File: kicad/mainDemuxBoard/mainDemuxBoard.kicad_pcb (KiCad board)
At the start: 2 copper layers, 217 parts, among them J1 Conn_02x20_Top_Bottom, J10 Conn_02x20_Top_Bottom, J11 Conn_02x20_Top_Bottom, J12 Conn_02x20_Top_Bottom, J13 Conn_02x20_Top_Bottom, J14 Conn_02x20_Top_Bottom, J15 Conn_02x20_Top_Bottom, J16 Conn_02x20_Top_Bottom, J17 Conn_02x20_Top_Bottom, J2 Conn_02x20_Top_Bottom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

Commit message: finish main demux board
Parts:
- moved J4 187.7 mm to (109.2, 105.0)
- moved J1 187.5 mm to (121.2, 105.0)
- moved J8 186.1 mm to (85.8, 105.0)
- moved J6 185.0 mm to (97.5, 105.0)
- moved J10 183.4 mm to (74.0, 105.0)
- moved J12 183.1 mm to (62.2, 105.0)
- moved J14 181.7 mm to (50.2, 105.0)
- moved J16 180.8 mm to (38.2, 105.0)
- moved J11 85.1 mm to (74.0, 32.0)
- moved J17 85.0 mm to (38.2, 32.0)
- moved J2 83.1 mm to (121.2, 32.0)
- moved J13 82.8 mm to (62.2, 32.0)
- moved J9 82.1 mm to (85.8, 32.0)
- moved J15 82.0 mm to (50.2, 32.0)
- moved J7 80.7 mm to (97.5, 32.0)
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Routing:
- net /S_{2}: track 0.00 -> 306.9 mm
- net /S_{3}: track 0.00 -> 297.1 mm, vias 0 -> 1
- net /S_{1}: track 0.00 -> 287.2 mm
- net /~{BL_{6}}: track 0.00 -> 284.4 mm, vias 0 -> 3
- net /BL_{1}: track 0.00 -> 284.2 mm
- net /~{BL_{5}}: track 0.00 -> 283.0 mm, vias 0 -> 2
- net /S_{0}: track 0.00 -> 281.1 mm
- net /~{BL_{4}}: track 0.00 -> 281.1 mm, vias 0 -> 1
- net /~{BL_{2}}: track 0.00 -> 278.9 mm, vias 0 -> 1
- net /~{BL_{0}}: track 0.00 -> 277.4 mm
- net /~{BL_{7}}: track 0.00 -> 277.2 mm
- net /~{BL_{1}}: track 0.00 -> 276.9 mm, vias 0 -> 2
- net /BL_{5}: track 0.00 -> 276.6 mm, vias 0 -> 1
- net /BL_{7}: track 0.00 -> 274.5 mm, vias 0 -> 2
- net /BL_{3}: track 0.00 -> 272.5 mm, vias 0 -> 1
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- added copper zone on In2.Cu, net +10V
- added copper zone on In2.Cu, net +5V
- added copper zone on In1.Cu, net GND
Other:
- board outline added: 150 x 150 mm
- copper layers 2 -> 4

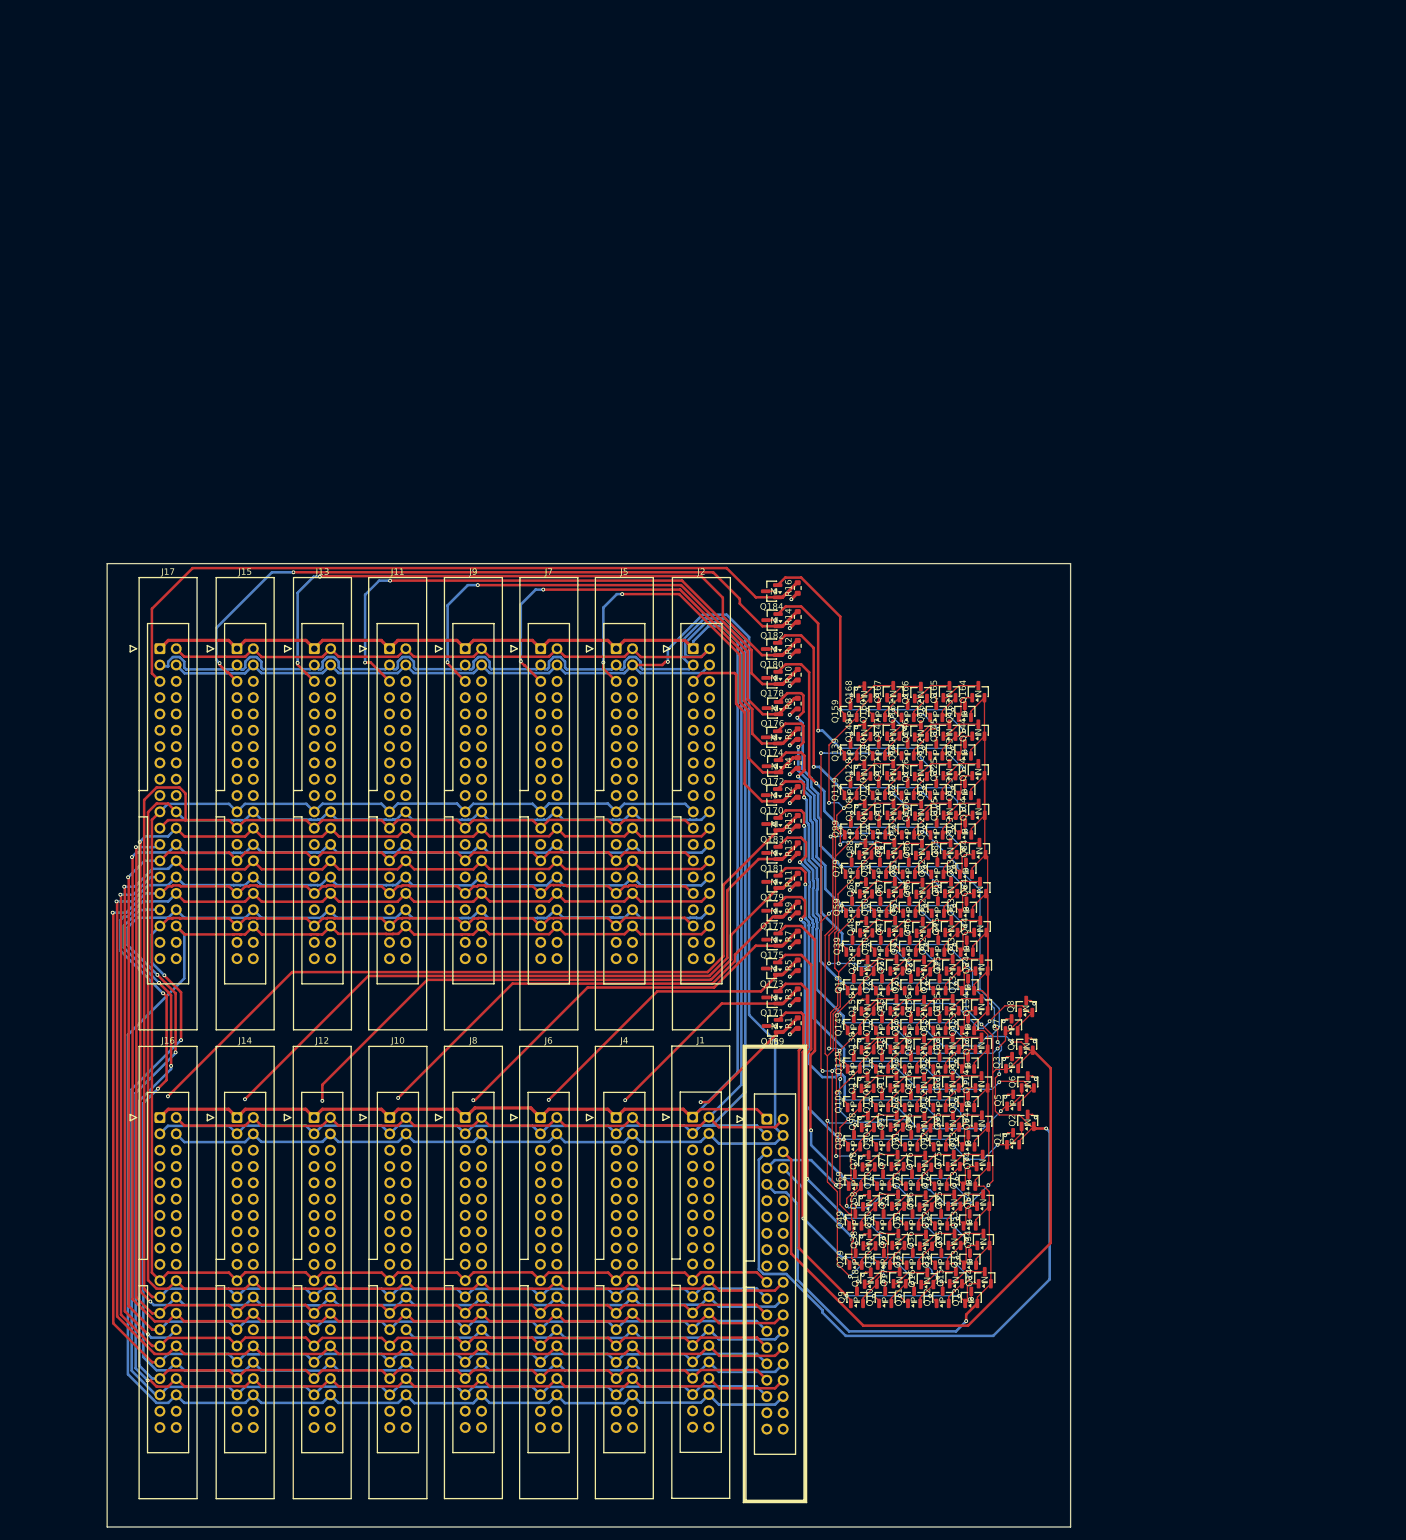
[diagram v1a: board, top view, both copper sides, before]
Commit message: update main board schematic
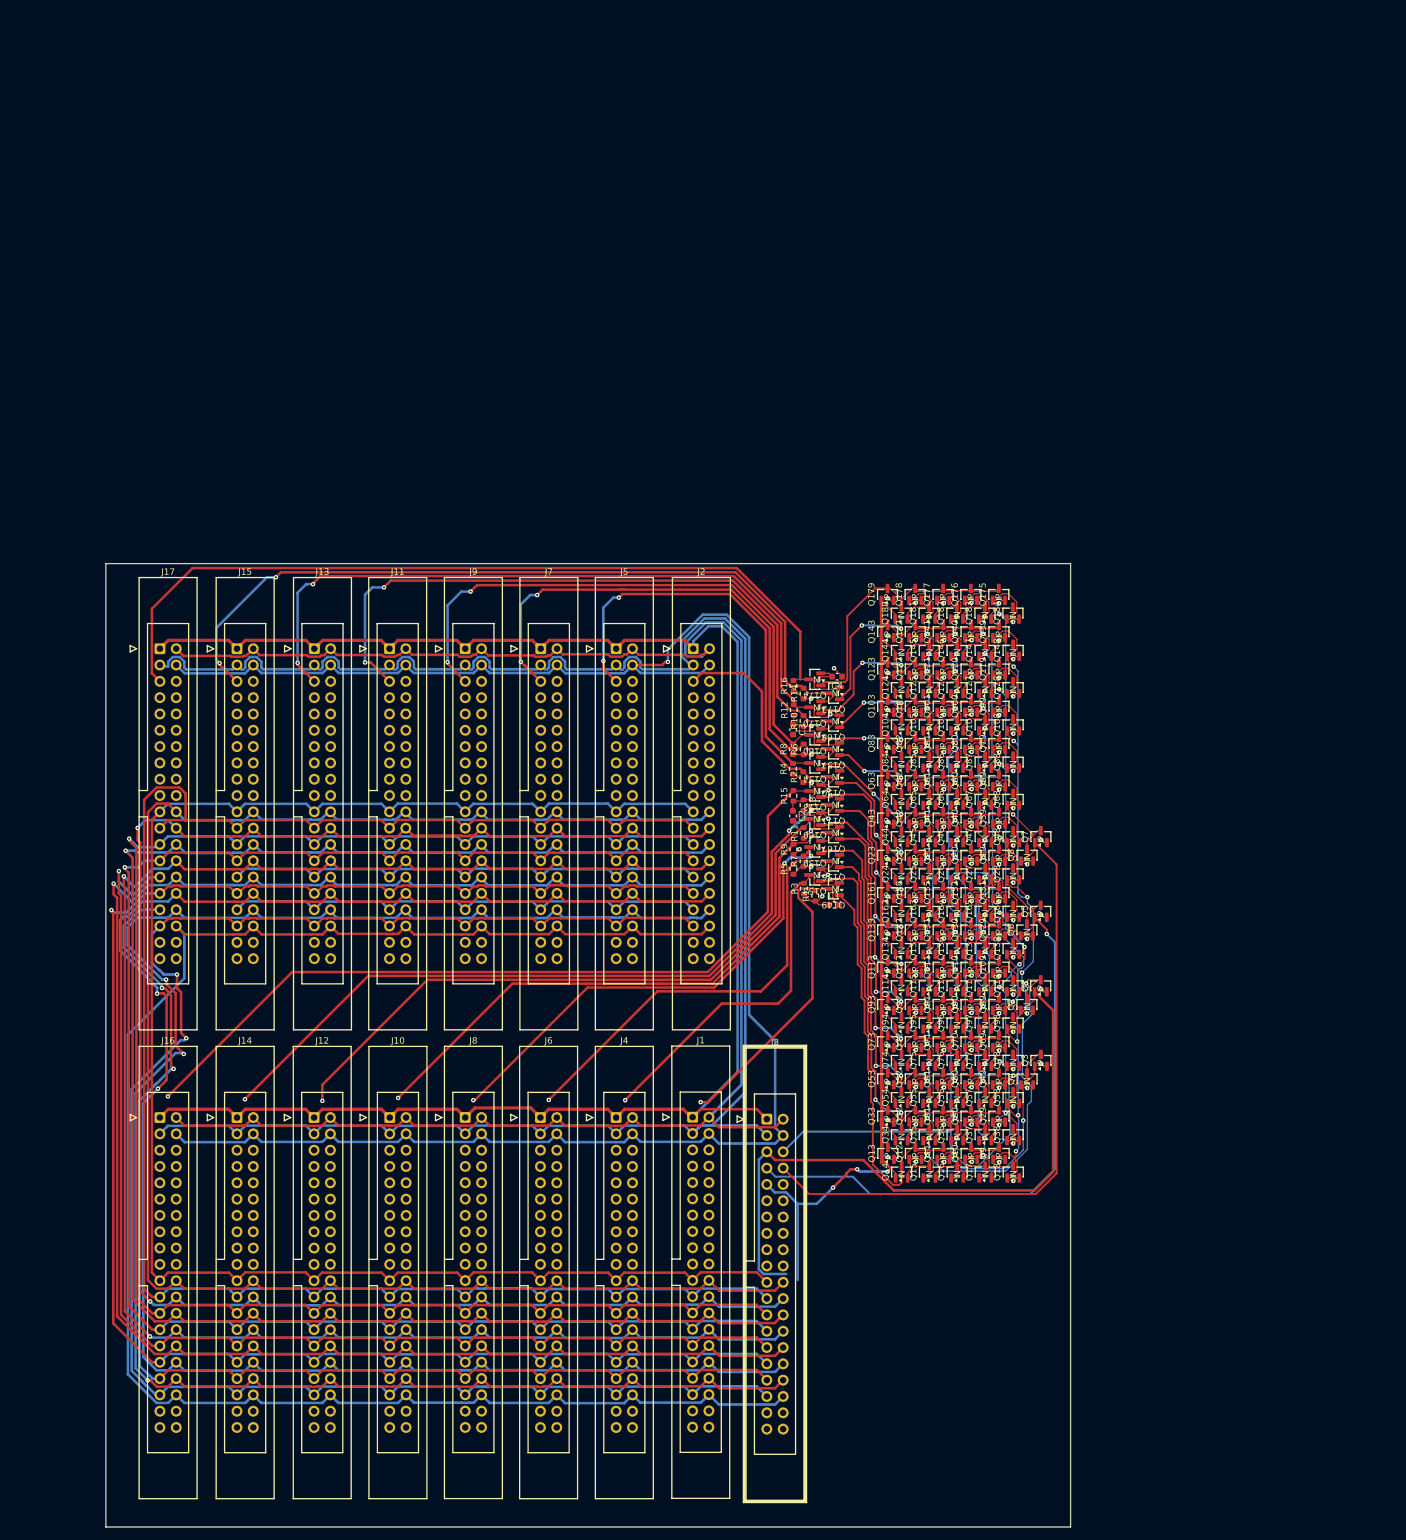
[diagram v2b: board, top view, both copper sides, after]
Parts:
- added C1: 100nC, Capacitor_SMD:C_0603_1608Metric, F.Cu at (143.2, 71.9)
- added C2: 100nC, Capacitor_SMD:C_0603_1608Metric, F.Cu at (136.8, 58.0)
- added C3: 100nC, Capacitor_SMD:C_0603_1608Metric, F.Cu at (136.8, 44.6)
- added C4: 100nC, Capacitor_SMD:C_0603_1608Metric, F.Cu at (143.6, 36.4)
- Q1, Q10, Q100, Q101, Q102, Q103, Q109, Q11, Q110, Q111, Q112, Q113, Q119, Q12, Q120, Q121, Q122, Q123, Q129, Q13, Q130, Q131, Q132, Q133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: value PMOS -> Q_PMOS_GSD
- Q104, Q105, Q106, Q107, Q108, Q114, Q115, Q116, Q117, Q118, Q124, Q125, Q126, Q127, Q128, Q134, Q135, Q136, Q137, Q138, Q14, Q144, Q145, Q146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: value NMOS -> Q_NMOS_GSD
- Q149, Q150, Q153, Q159, Q160, Q162, Q163: value PMOS -> Q_NMOS_GSD; footprint easyeda2kicad:SOT-23-P -> easyeda2kicad:SOT-23-N
- Q155, Q158, Q175, Q176, Q177, Q178, Q179: value NMOS -> Q_PMOS_GSD; footprint easyeda2kicad:SOT-23-N -> easyeda2kicad:SOT-23-P
- moved Q175 64.4 mm to (168.8, 23.5), turned to 90 degrees
- moved Q177 56.0 mm to (160.2, 23.5), turned to 90 degrees
- moved Q179 48.3 mm to (151.5, 23.5), turned to 90 degrees
- moved Q183 46.7 mm to (166.7, 26.4), turned to 90 degrees
- moved Q154 45.8 mm to (140.1, 49.8), turned to 180 degrees
- moved Q181 44.7 mm to (158.0, 26.4), turned to 90 degrees
- moved Q157 41.0 mm to (143.0, 47.6), turned to 180 degrees
- moved Q150 39.3 mm to (143.0, 52.0), turned to 180 degrees
- moved Q184 37.7 mm to (171.0, 26.4), turned to 90 degrees
- moved Q166 36.9 mm to (171.1, 72.8)
- moved Q176 35.6 mm to (164.5, 23.5), turned to 90 degrees
- moved Q165 34.6 mm to (166.7, 72.8)
- moved Q164 34.3 mm to (162.3, 72.8)
- moved Q153 33.4 mm to (140.1, 67.2), turned to 180 degrees
- moved Q169 32.9 mm to (140.1, 58.5)
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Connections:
- Q1 pad 1: /1_16_5V_DEMUX_NOTOUT/5VNOT/Y -> /1_16_5V_DEMUX_NOTOUT/S_{0}
- Q1 pad 2: /1_16_5V_DEMUX_NOTOUT/S_{0} -> +5V
- Q1 pad 3: +5V -> /1_16_5V_DEMUX_NOTOUT/5VNOT/Y
- Q10 pad 1: /16_NOT/A_{0} -> /1_16_5V_DEMUX_NOTOUT/5VNOT2/Y
- Q10 pad 2: /1_16_5V_DEMUX_NOTOUT/5VNOT2/Y -> +5V
- Q10 pad 3: +5V -> /16_NOT/A_{0}
- Q100 pad 1: /16_NOT/A_{12} -> /1_16_5V_DEMUX_NOTOUT/5VNOT2/Y
- Q100 pad 2: /1_16_5V_DEMUX_NOTOUT/5VNOT2/Y -> +5V
- Q100 pad 3: +5V -> /16_NOT/A_{12}
- Q101 pad 1: /16_NOT/A_{12} -> /1_16_5V_DEMUX_NOTOUT/S_{1}
- Q101 pad 2: /1_16_5V_DEMUX_NOTOUT/S_{1} -> +5V
- Q101 pad 3: +5V -> /16_NOT/A_{12}
- Q102 pad 1: /16_NOT/A_{12} -> /1_16_5V_DEMUX_NOTOUT/S_{0}
- Q102 pad 2: /1_16_5V_DEMUX_NOTOUT/S_{0} -> +5V
- Q102 pad 3: +5V -> /16_NOT/A_{12}
- Q103 pad 1: /16_NOT/A_{12} -> /1_16_5V_DEMUX_NOTOUT/D
- Q103 pad 2: /1_16_5V_DEMUX_NOTOUT/D -> +5V
- Q103 pad 3: +5V -> /16_NOT/A_{12}
- Q104 pad 1: /16_NOT/A_{12} -> /1_16_5V_DEMUX_NOTOUT/D
- Q104 pad 2: /1_16_5V_DEMUX_NOTOUT/D -> Net-(Q104-S)
- Q104 pad 3: Net-(Q104-S) -> /16_NOT/A_{12}
- Q105 pad 1: Net-(Q104-S) -> /1_16_5V_DEMUX_NOTOUT/S_{0}
- Q105 pad 2: /1_16_5V_DEMUX_NOTOUT/S_{0} -> Net-(Q105-S)
- Q105 pad 3: Net-(Q105-S) -> Net-(Q104-S)
- Q106 pad 1: Net-(Q105-S) -> /1_16_5V_DEMUX_NOTOUT/S_{1}
- Q106 pad 2: /1_16_5V_DEMUX_NOTOUT/S_{1} -> Net-(Q106-S)
- Q106 pad 3: Net-(Q106-S) -> Net-(Q105-S)
- Q107 pad 1: Net-(Q106-S) -> /1_16_5V_DEMUX_NOTOUT/5VNOT2/Y
- Q107 pad 2: /1_16_5V_DEMUX_NOTOUT/5VNOT2/Y -> Net-(Q107-S)
- Q107 pad 3: Net-(Q107-S) -> Net-(Q106-S)
- Q108 pad 1: Net-(Q107-S) -> /1_16_5V_DEMUX_NOTOUT/5VNOT3/Y
- Q108 pad 2: /1_16_5V_DEMUX_NOTOUT/5VNOT3/Y -> GND
- Q108 pad 3: GND -> Net-(Q107-S)
- Q109 pad 1: /16_NOT/A_{5} -> /1_16_5V_DEMUX_NOTOUT/S_{3}
- Q109 pad 2: /1_16_5V_DEMUX_NOTOUT/S_{3} -> +5V
- Q109 pad 3: +5V -> /16_NOT/A_{5}
- Q11 pad 1: /16_NOT/A_{0} -> /1_16_5V_DEMUX_NOTOUT/5VNOT1/Y
- Q11 pad 2: /1_16_5V_DEMUX_NOTOUT/5VNOT1/Y -> +5V
- Q11 pad 3: +5V -> /16_NOT/A_{0}
- Q110 pad 1: /16_NOT/A_{5} -> /1_16_5V_DEMUX_NOTOUT/5VNOT2/Y
- Q110 pad 2: /1_16_5V_DEMUX_NOTOUT/5VNOT2/Y -> +5V
- Q110 pad 3: +5V -> /16_NOT/A_{5}
- Q111 pad 1: /16_NOT/A_{5} -> /1_16_5V_DEMUX_NOTOUT/S_{1}
- Q111 pad 2: /1_16_5V_DEMUX_NOTOUT/S_{1} -> +5V
- Q111 pad 3: +5V -> /16_NOT/A_{5}
- Q112 pad 1: /16_NOT/A_{5} -> /1_16_5V_DEMUX_NOTOUT/5VNOT/Y
- Q112 pad 2: /1_16_5V_DEMUX_NOTOUT/5VNOT/Y -> +5V
- Q112 pad 3: +5V -> /16_NOT/A_{5}
- Q113 pad 1: /16_NOT/A_{5} -> /1_16_5V_DEMUX_NOTOUT/D
- Q113 pad 2: /1_16_5V_DEMUX_NOTOUT/D -> +5V
- Q113 pad 3: +5V -> /16_NOT/A_{5}
- Q114 pad 1: /16_NOT/A_{5} -> /1_16_5V_DEMUX_NOTOUT/D
- Q114 pad 2: /1_16_5V_DEMUX_NOTOUT/D -> Net-(Q114-S)
- Q114 pad 3: Net-(Q114-S) -> /16_NOT/A_{5}
- Q115 pad 1: Net-(Q114-S) -> /1_16_5V_DEMUX_NOTOUT/5VNOT/Y
- Q115 pad 2: /1_16_5V_DEMUX_NOTOUT/5VNOT/Y -> Net-(Q115-S)
- Q115 pad 3: Net-(Q115-S) -> Net-(Q114-S)
- Q116 pad 1: Net-(Q115-S) -> /1_16_5V_DEMUX_NOTOUT/S_{1}
- Q116 pad 2: /1_16_5V_DEMUX_NOTOUT/S_{1} -> Net-(Q116-S)
- Q116 pad 3: Net-(Q116-S) -> Net-(Q115-S)
- Q117 pad 1: Net-(Q116-S) -> /1_16_5V_DEMUX_NOTOUT/5VNOT2/Y
- Q117 pad 2: /1_16_5V_DEMUX_NOTOUT/5VNOT2/Y -> Net-(Q117-S)
- Q117 pad 3: Net-(Q117-S) -> Net-(Q116-S)
- Q118 pad 1: Net-(Q117-S) -> /1_16_5V_DEMUX_NOTOUT/S_{3}
- Q118 pad 2: /1_16_5V_DEMUX_NOTOUT/S_{3} -> GND
- Q118 pad 3: GND -> Net-(Q117-S)
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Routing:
- net /BL_{4}: track 183.8 -> 280.6 mm
- net /BL_{2}: track 181.7 -> 275.3 mm
- net /BL_{6}: track 187.2 -> 278.5 mm
- net +10V: track 211.6 -> 299.6 mm
- net /1_16_5V_DEMUX_NOTOUT/S_{3}: track 200.0 -> 271.6 mm, vias 11 -> 10
- net /1_16_5V_DEMUX_NOTOUT/D: track 251.6 -> 194.4 mm, vias 1 -> 3
- net GND: track 52.7 -> 106.2 mm, vias 36 -> 24
- net /1_16_5V_DEMUX_NOTOUT/5VNOT/Y: track 85.3 -> 137.9 mm
- net /1_16_5V_DEMUX_NOTOUT/5VNOT2/Y: track 202.3 -> 151.4 mm, vias 15 -> 10
- net /~{BL_{3}}: track 240.6 -> 282.0 mm
- net /1_16_5V_DEMUX_NOTOUT/S_{0}: track 210.3 -> 250.0 mm, vias 18 -> 15
- net /1_16_5V_DEMUX_NOTOUT/S_{1}: track 227.6 -> 191.8 mm
- net /16_NOT/A_{10}: track 66.0 -> 33.3 mm, vias 6 -> 2
- net /16_NOT/A_{11}: track 64.8 -> 35.0 mm, vias 6 -> 2
- net /16_NOT/A_{8}: track 68.7 -> 39.2 mm, vias 6 -> 2
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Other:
- board size 150 x 150 mm -> 150.2 x 150 mm
